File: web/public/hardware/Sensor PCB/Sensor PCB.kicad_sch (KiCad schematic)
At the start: 32 parts, among them J1 Conn_01x08_Pin, J2 Conn_01x08_Pin, J3 Conn_01x02_Pin, J4 Conn_01x02_Pin, U1 DRV5033FAQDBZR, U2 DRV5033AJxDBZ, U3 DRV5033FAQDBZR, U4 DRV5033AJxDBZ, U5 CD74HCT11, U6 CD74HCT11

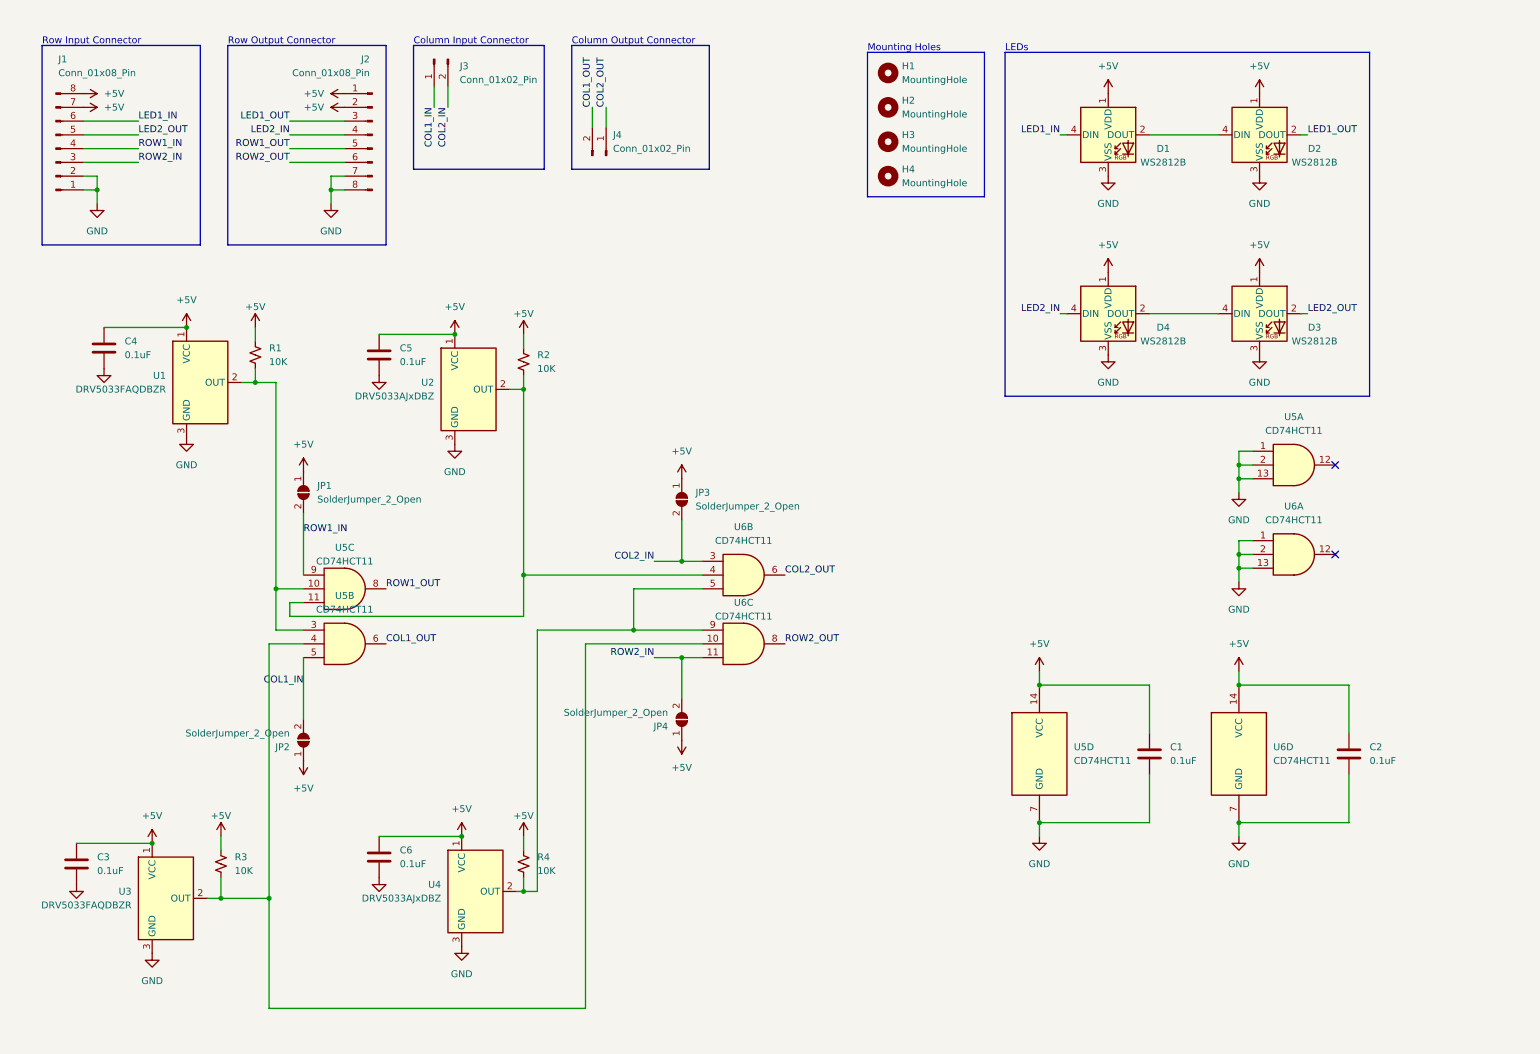
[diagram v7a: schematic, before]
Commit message: Connected Hall Effect Sensors to Bus
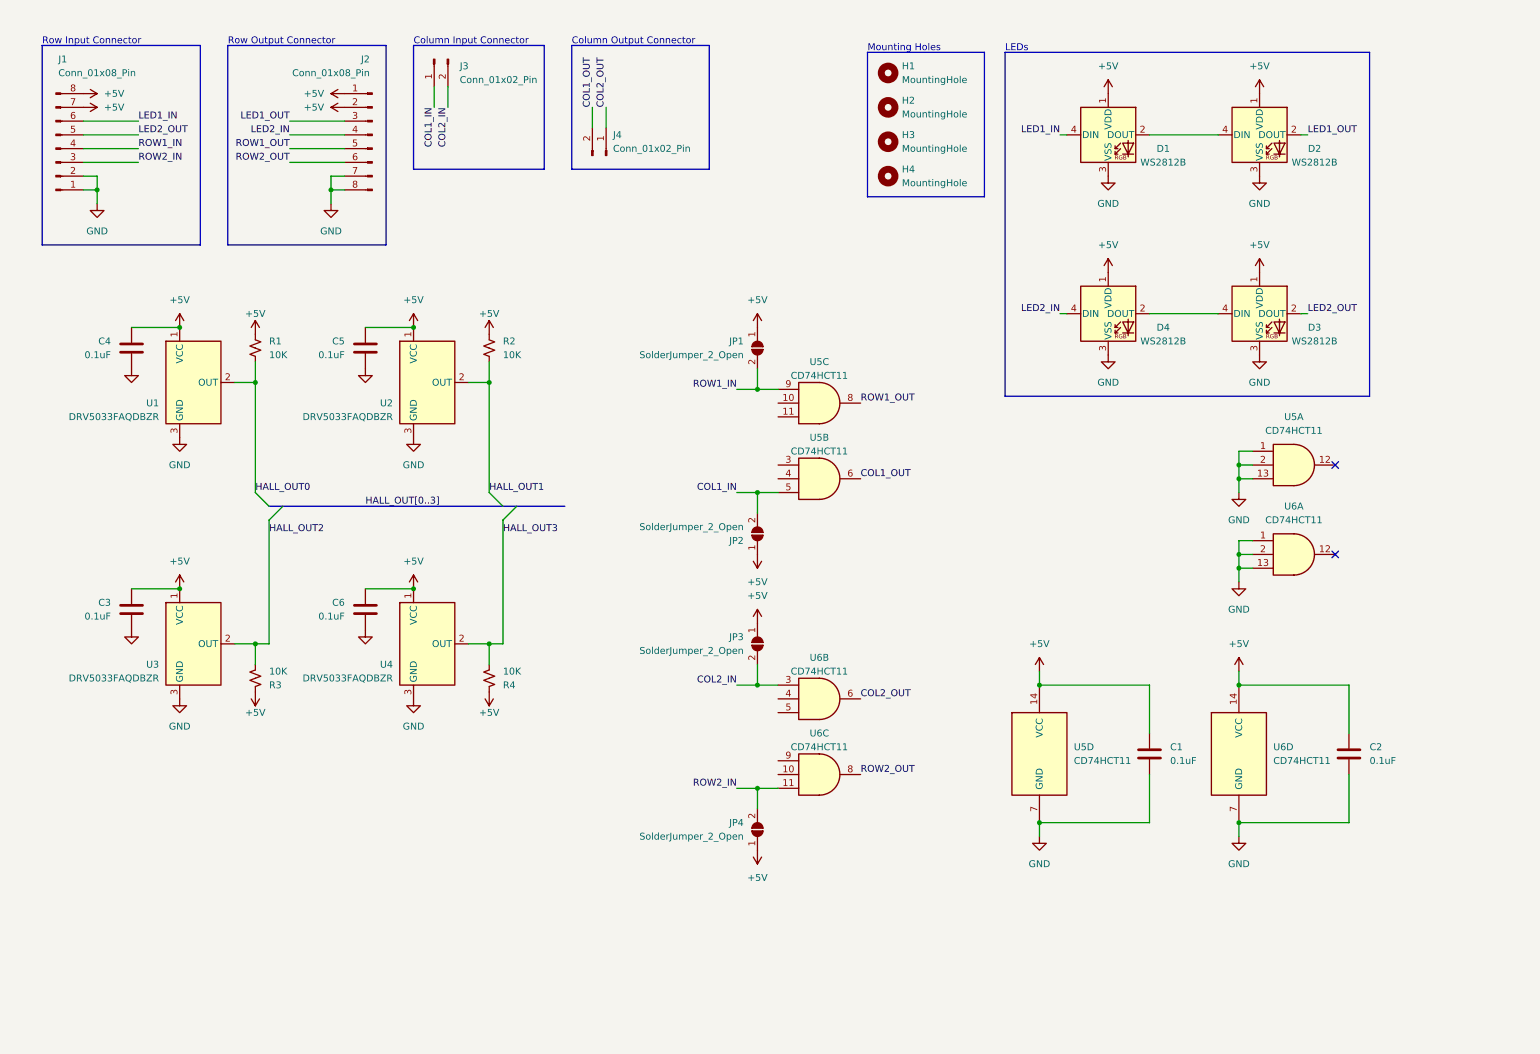
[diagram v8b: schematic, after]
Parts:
- U2, U4: value DRV5033AJxDBZ -> DRV5033FAQDBZR
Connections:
- net HALL_OUT1: now reaches R2.2, U2.2 (OUT)
- net HALL_OUT1: no longer U5.11, U6.4
- net HALL_OUT3: now reaches R4.2, U4.2 (OUT)
- net HALL_OUT3: no longer U6.5, U6.9
- net HALL_OUT0: now reaches R1.2, U1.2 (OUT)
- net HALL_OUT0: no longer U5.10, U5.3
- net HALL_OUT2: now reaches R3.2, U3.2 (OUT)
- net HALL_OUT2: no longer U5.4, U6.10
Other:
- moved on the sheet: C3, C4, C5, C6, JP1, JP2, JP3, JP4, R1, R2, R3, R4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
